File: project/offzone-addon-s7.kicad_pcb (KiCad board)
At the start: 2 copper layers, 43.8 x 44.1 mm, 0 parts

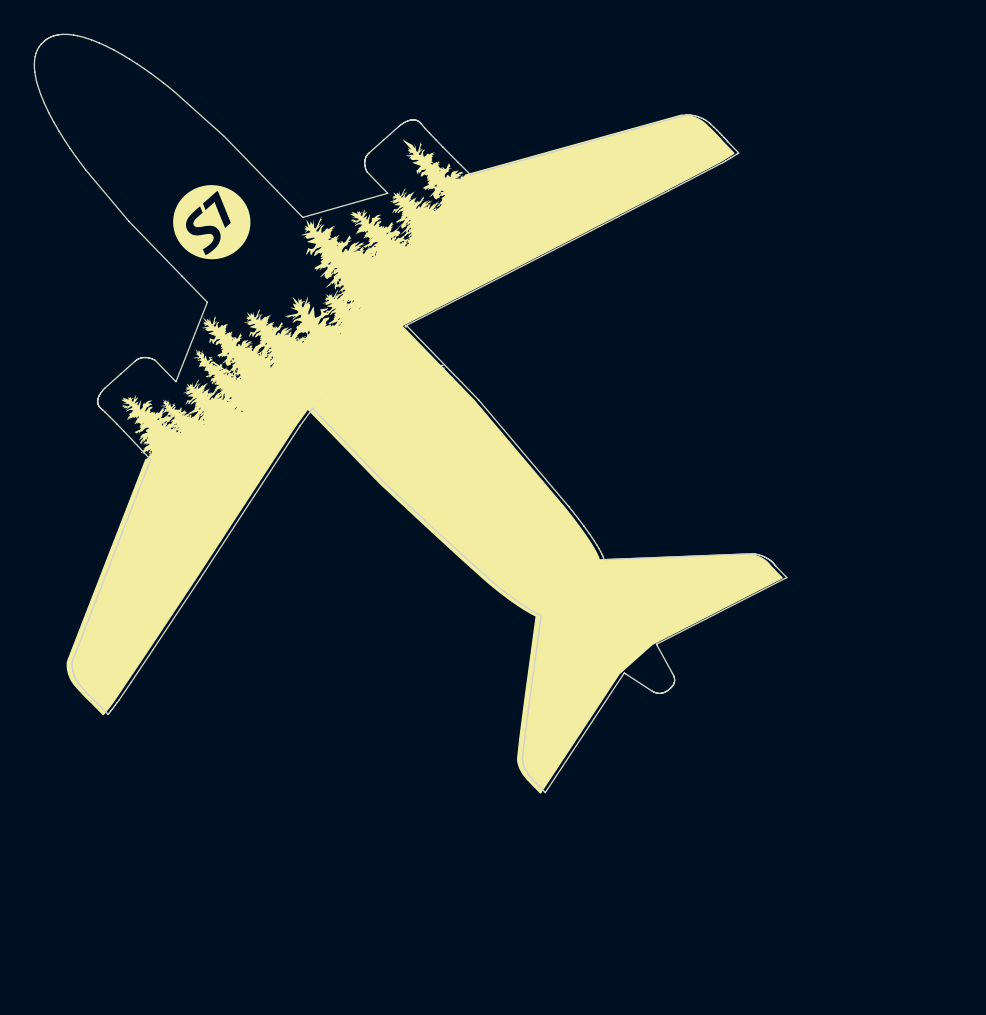
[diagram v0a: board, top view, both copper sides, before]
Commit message: Fix size to 50mm
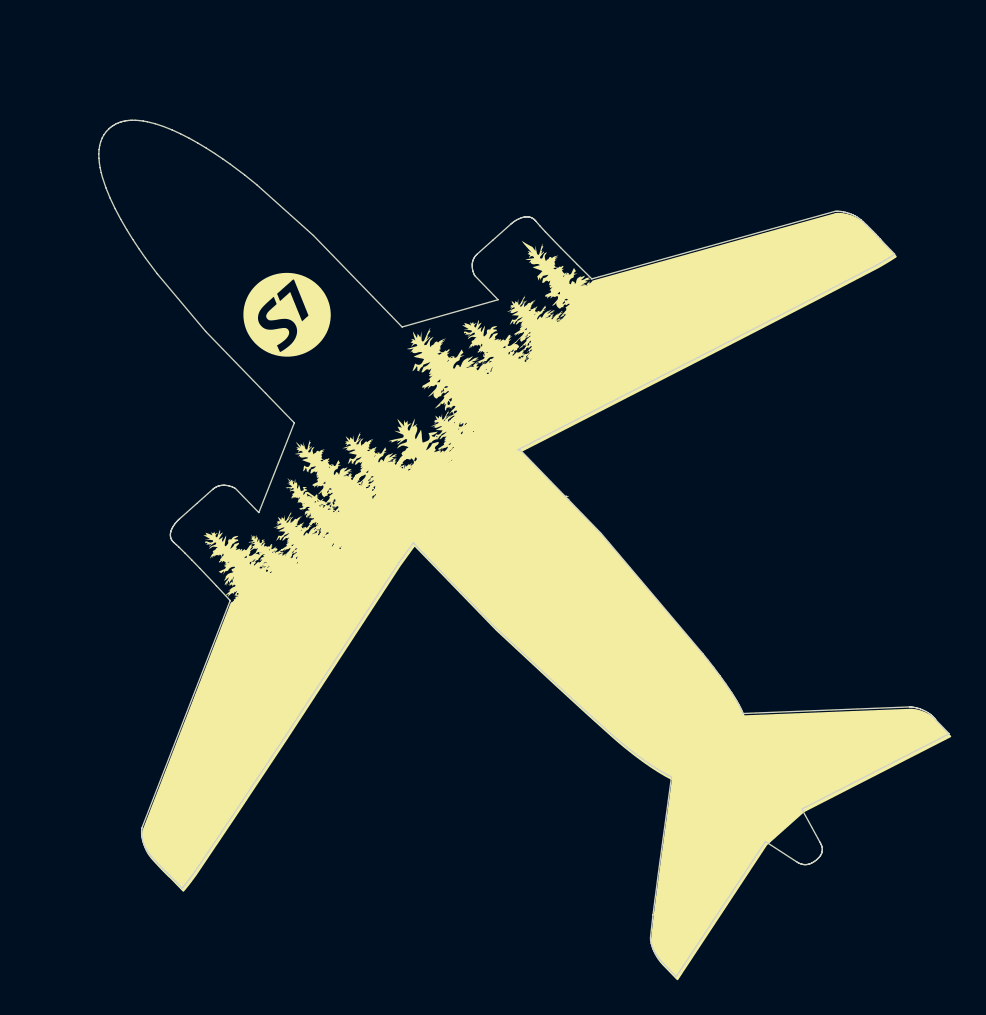
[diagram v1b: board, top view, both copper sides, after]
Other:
- board size 43.8 x 44.1 mm -> 49.5 x 49.9 mm
